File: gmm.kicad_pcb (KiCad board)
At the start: 6 copper layers, 70 x 50 mm, 213 parts, among them P1 10144518-061802LF, P2 10144518-061802LF, P3 10144518-061802LF, P4 10144518-061802LF, P5 10144518-061802LF, U1 CCGM1A1, U10 PCA9539AHF, U11 TPS3840DL28DBV, U2 5P49V6965, U3 LM26480SQ, U4 STG3692, U5 STG3692, U6 74LVC1G08, U7 74LVC1G07, U8 STG3692, U9 IS25LQ032B-JNLE, Y1 NX3225SA

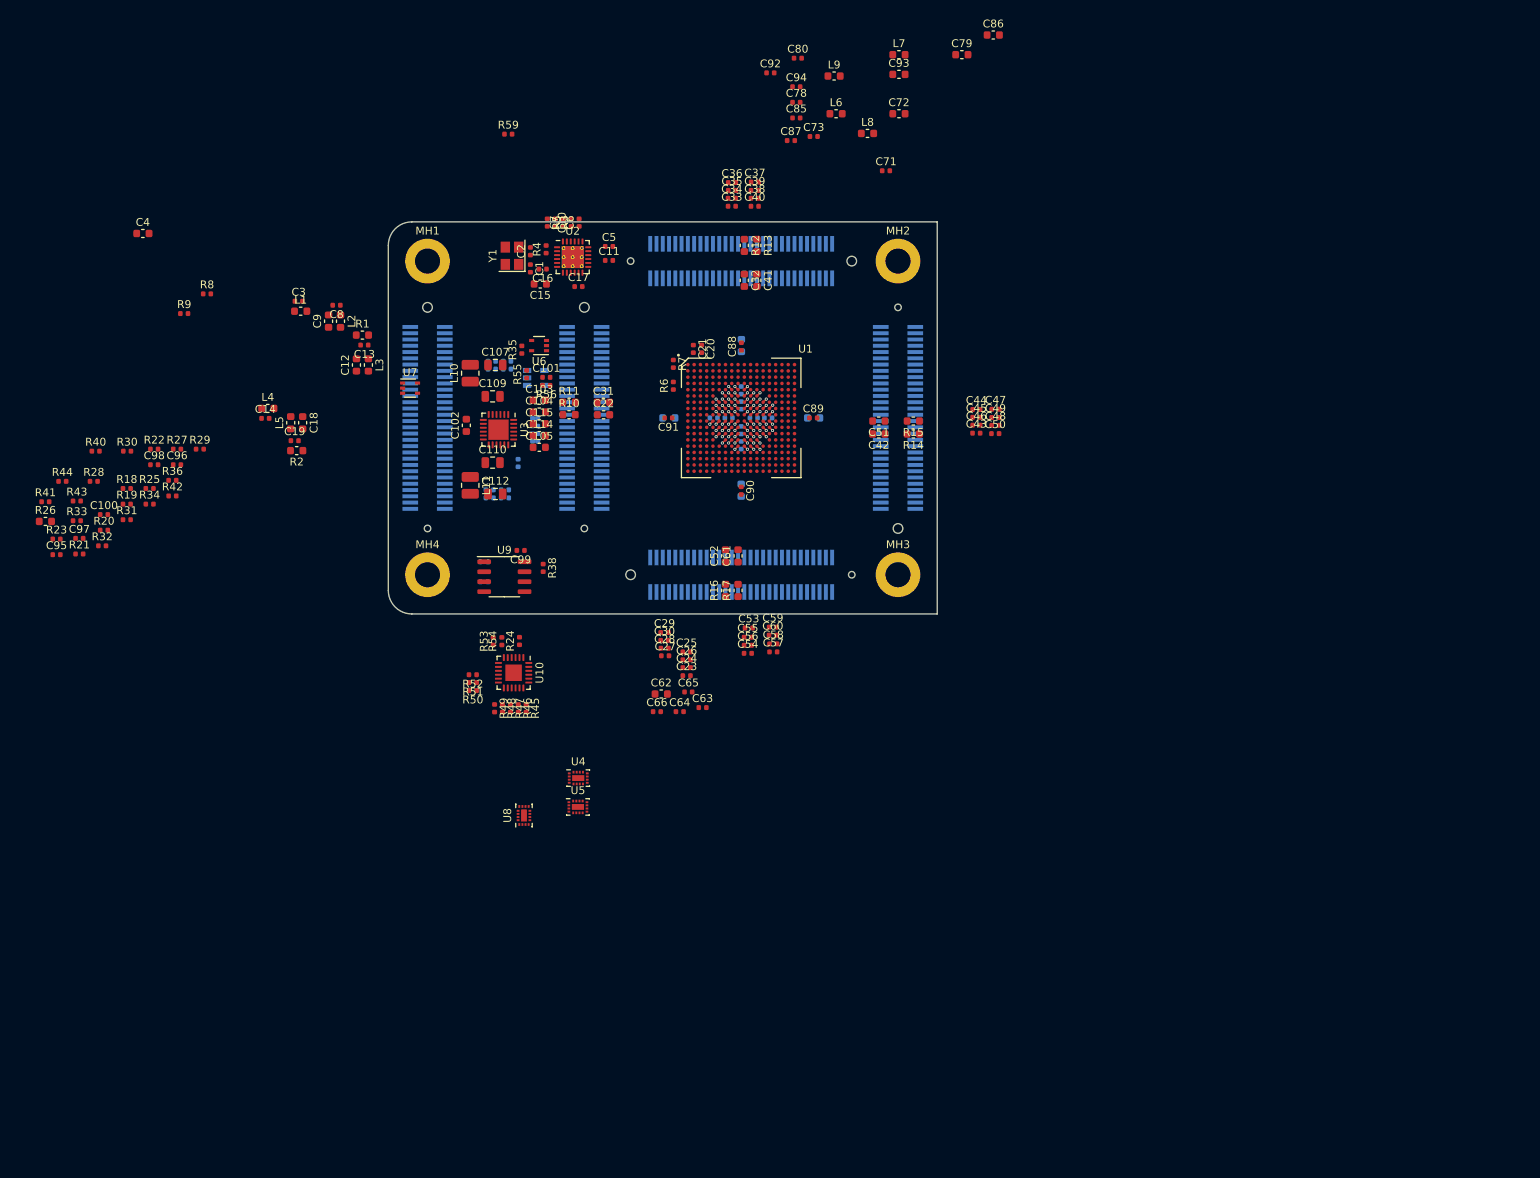
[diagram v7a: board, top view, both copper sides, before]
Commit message: Add footprints for solder jumpers and L10 inductor
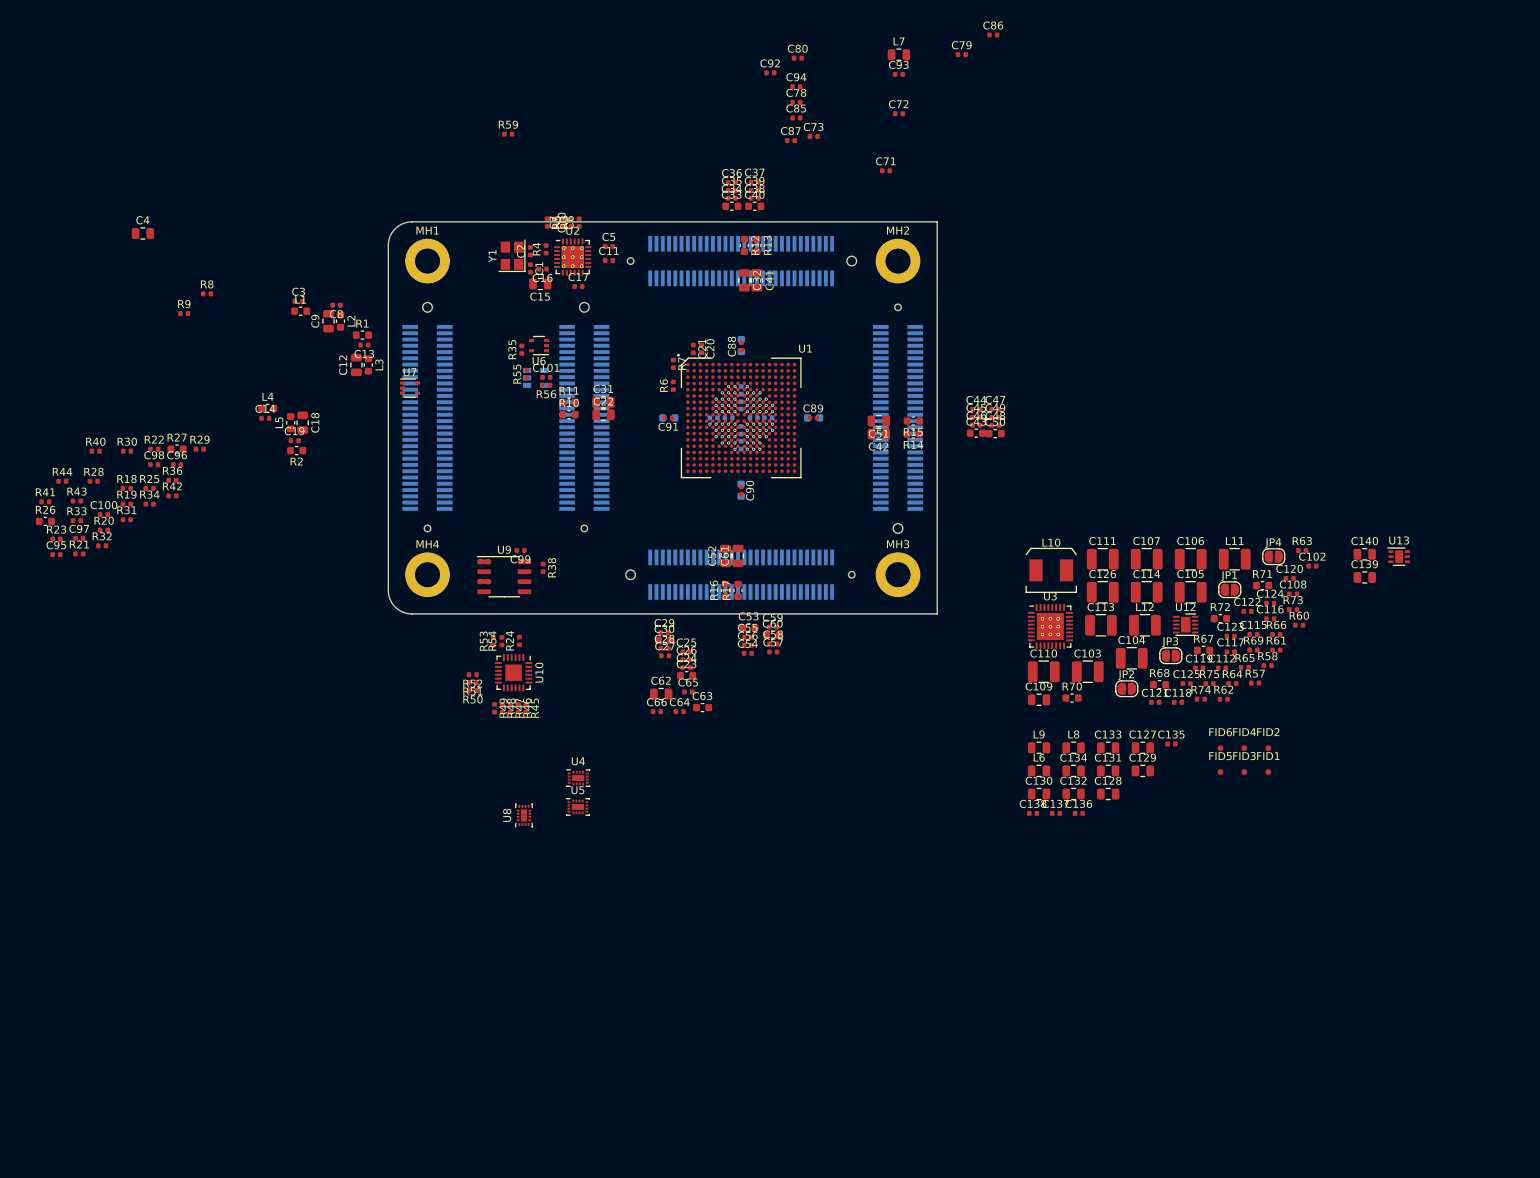
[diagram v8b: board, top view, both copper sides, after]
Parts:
- added C116: 0.01uF, Capacitor_SMD:C_0402_1005Metric, F.Cu at (202.5, 130.6)
- added C117: 0.01uF, Capacitor_SMD:C_0402_1005Metric, F.Cu at (197.4, 134.8)
- added C118: DNI, Capacitor_SMD:C_0402_1005Metric, F.Cu at (190.7, 141.3)
- added C119: 1000pF, Capacitor_SMD:C_0402_1005Metric, F.Cu at (193.4, 136.9)
- added C120: DNI, Capacitor_SMD:C_0402_1005Metric, F.Cu at (204.9, 125.5)
- added C121: 1000pF, Capacitor_SMD:C_0402_1005Metric, F.Cu at (187.8, 141.3)
- added C122: 0.01uF, Capacitor_SMD:C_0402_1005Metric, F.Cu at (199.6, 129.7)
- added C123: DNI, Capacitor_SMD:C_0402_1005Metric, F.Cu at (197.4, 132.8)
- added C124: 1000pF, Capacitor_SMD:C_0402_1005Metric, F.Cu at (202.5, 128.6)
- added C125: 0.1uF, Capacitor_SMD:C_0402_1005Metric, F.Cu at (191.8, 138.9)
- added C126: 22uF, Capacitor_SMD:C_1210_3225Metric, F.Cu at (181.1, 127.2)
- added C127: 2.2uF, Capacitor_SMD:C_0805_2012Metric, F.Cu at (186.2, 147.1)
- added C128: 2.2uF, Capacitor_SMD:C_0805_2012Metric, F.Cu at (181.8, 153.0)
- added C129: 2.2uF, Capacitor_SMD:C_0805_2012Metric, F.Cu at (186.2, 150.0)
- added C130: 2.2uF, Capacitor_SMD:C_0805_2012Metric, F.Cu at (173.0, 153.0)
- added C131: 2.2uF, Capacitor_SMD:C_0805_2012Metric, F.Cu at (181.8, 150.0)
- added C132: 2.2uF, Capacitor_SMD:C_0805_2012Metric, F.Cu at (177.4, 153.0)
- added C133: 2.2uF, Capacitor_SMD:C_0805_2012Metric, F.Cu at (181.8, 147.1)
- added C134: 2.2uF, Capacitor_SMD:C_0805_2012Metric, F.Cu at (177.4, 150.0)
- added C135: 0.1uF, Capacitor_SMD:C_0402_1005Metric, F.Cu at (189.9, 146.6)
- added C136: 0.1uF, Capacitor_SMD:C_0402_1005Metric, F.Cu at (178.1, 155.4)
- added C137: 0.01uF, Capacitor_SMD:C_0402_1005Metric, F.Cu at (175.1, 155.4)
- added C138: 0.01uF, Capacitor_SMD:C_0402_1005Metric, F.Cu at (172.2, 155.4)
- added C139: 2.2uF, Capacitor_SMD:C_0805_2012Metric, F.Cu at (214.5, 125.3)
- added C140: 2.2uF, Capacitor_SMD:C_0805_2012Metric, F.Cu at (214.5, 122.4)
- added FID1: Fiducial, Fiducial:Fiducial_0.75mm_Mask1.5mm, F.Cu at (202.2, 150.2)
- added FID2: Fiducial, Fiducial:Fiducial_0.75mm_Mask1.5mm, F.Cu at (202.2, 147.1)
- added FID3: Fiducial, Fiducial:Fiducial_0.75mm_Mask1.5mm, F.Cu at (199.2, 150.2)
- added FID4: Fiducial, Fiducial:Fiducial_0.75mm_Mask1.5mm, F.Cu at (199.2, 147.1)
- added FID5: Fiducial, Fiducial:Fiducial_0.75mm_Mask1.5mm, F.Cu at (196.1, 150.2)
- added FID6: Fiducial, Fiducial:Fiducial_0.75mm_Mask1.5mm, F.Cu at (196.1, 147.1)
- added JP1: SolderJumper_2_Open_Small, Jumper:SolderJumper-2_P1.3mm_Open_RoundedPad1.0x1.5mm, F.Cu at (197.3, 126.9)
- added JP2: SolderJumper_2_Open_Small, Jumper:SolderJumper-2_P1.3mm_Open_RoundedPad1.0x1.5mm, F.Cu at (184.2, 139.5)
- added JP3: SolderJumper_2_Open_Small, Jumper:SolderJumper-2_P1.3mm_Open_RoundedPad1.0x1.5mm, F.Cu at (189.8, 135.3)
- added JP4: SolderJumper_2_Open_Small, Jumper:SolderJumper-2_P1.3mm_Open_RoundedPad1.0x1.5mm, F.Cu at (202.9, 122.7)
- added L12: 2.2uH, Inductor_SMD:L_1210_3225Metric, F.Cu at (186.5, 131.4)
- added R67: 10k, Resistor_SMD:R_0603_1608Metric, F.Cu at (194.0, 134.6)
- added R68: 20k, Resistor_SMD:R_0603_1608Metric, F.Cu at (188.4, 139.0)
- added R69: 2k, Resistor_SMD:R_0402_1005Metric, F.Cu at (200.3, 134.6)
- added R70: 0, Resistor_SMD:R_0603_1608Metric, F.Cu at (177.2, 140.7)
- added R71: DNI, Resistor_SMD:R_0603_1608Metric, F.Cu at (201.5, 126.4)
- added R72: 20k, Resistor_SMD:R_0603_1608Metric, F.Cu at (196.1, 130.6)
- added R73: 2k, Resistor_SMD:R_0402_1005Metric, F.Cu at (205.4, 129.4)
- added R74: 2k, Resistor_SMD:R_0402_1005Metric, F.Cu at (193.6, 140.9)
- added R75: 16k, Resistor_SMD:R_0402_1005Metric, F.Cu at (194.7, 138.9)
- added U12: TPS7A91, Package_DFN_QFN:Texas_S-PDSO-N10_EP1.2x2mm, F.Cu at (191.7, 131.4)
- added U13: ADP151ACP, Package_DFN_QFN:DFN-6-1EP_2x2mm_P0.65mm_EP1x1.6mm, F.Cu at (218.9, 122.7)
- C10, C11, C16, C17, C24, C25, C26, C27, C28, C29, C34, C35, C36, C37, C38, C39, C44, C45, C46, C47, C48, C49, C5, C54, C55, C56, C57, C58, C59, C6, C64, C65, C66, C7, C74, C75, C81, C82, C88, C89: value 0.01uF -> 0.1uF
- C102: value 1.0uF -> 0.047uF; footprint Capacitor_SMD:C_0603_1608Metric -> Capacitor_SMD:C_0402_1005Metric
- C103, C104, C105, C114: value 1.0uF -> 22uF; footprint Capacitor_SMD:C_0603_1608Metric -> Capacitor_SMD:C_1210_3225Metric
- C106: value 15pF -> 22uF; footprint Capacitor_SMD:C_0402_1005Metric -> Capacitor_SMD:C_1210_3225Metric; moved to F.Cu
- C107, C110: value 10uF -> 22uF; footprint Capacitor_SMD:C_0805_2012Metric -> Capacitor_SMD:C_1210_3225Metric
- C108: value DNI -> 0.047uF; moved to F.Cu
- C109: value 10uF -> 2.2uF
- C111: value 8.2pF -> 22uF; footprint Capacitor_SMD:C_0402_1005Metric -> Capacitor_SMD:C_1210_3225Metric; moved to F.Cu
- C112: value 10uF -> 0.047uF; footprint Capacitor_SMD:C_0805_2012Metric -> Capacitor_SMD:C_0402_1005Metric
- C113: value DNI -> 22uF; footprint Capacitor_SMD:C_0402_1005Metric -> Capacitor_SMD:C_1210_3225Metric; moved to F.Cu
- C115: value 1.0uF -> 0.01uF; footprint Capacitor_SMD:C_0603_1608Metric -> Capacitor_SMD:C_0402_1005Metric
- C12, C15, C18, C22, C31, C32, C4, C41, C42, C51, C52, C61, C62, C9: value 1.0uF -> 2.2uF; footprint Capacitor_SMD:C_0603_1608Metric -> Capacitor_SMD:C_0805_2012Metric
- C23, C30, C33, C40, C43, C50, C53, C60, C63: value 0.01uF -> 0.47uF; footprint Capacitor_SMD:C_0402_1005Metric -> Capacitor_SMD:C_0603_1608Metric
- C67, C68, C69, C70: value 1.0uF -> 0.47uF
- C72, C79, C86, C93: value 1.0uF -> 0.1uF; footprint Capacitor_SMD:C_0603_1608Metric -> Capacitor_SMD:C_0402_1005Metric
- L10: footprint Inductor_SMD:L_1008_2520Metric -> gmm:L_Murata_FDSD0518_5.2x4.9mm
- L11: footprint Inductor_SMD:L_1008_2520Metric -> Inductor_SMD:L_1210_3225Metric
- L6, L7, L8, L9: value 4.7uH -> 600 Ohm @100MHz, 1.5A; footprint Inductor_SMD:L_0603_1608Metric -> Inductor_SMD:L_0805_2012Metric
- R27: footprint Resistor_SMD:R_0402_1005Metric -> Resistor_SMD:R_0603_1608Metric
- R37, R38, R39: value 4.7k -> 10k
- R57, R58: value 100k -> 2.49k; moved to F.Cu
- R60: value 402k -> 23.7k; moved to F.Cu
- R61: value 100k -> 7.5k; moved to F.Cu
- R62: value 10k -> 7.5k; moved to F.Cu
- R63, R64: value 100k -> 15k; moved to F.Cu
- R65, R66: value 100k -> 10k; moved to F.Cu
- U3: value LM26480SQ -> TPS65266; footprint Package_DFN_QFN:WQFN-24-1EP_4x4mm_P0.5mm_EP2.6x2.6mm -> Package_DFN_QFN:Texas_S-PVQFN-N32_EP3.45x3.45mm_ThermalVias
- moved C102 109.4 mm to (207.9, 123.9), turned to 0 degrees
- moved R57 105.6 mm to (200.5, 138.8)
- moved R60 104.5 mm to (206.2, 131.4)
- moved R58 104.5 mm to (202.1, 136.6)
- moved C108 104.3 mm to (205.4, 127.5)
- moved R61 100.3 mm to (203.2, 134.6)
- moved R63 99.2 mm to (206.5, 121.9), turned to 0 degrees
- moved R66 98.0 mm to (203.2, 132.6), turned to 0 degrees
- moved L11 97.9 mm to (197.9, 123.0), turned to 0 degrees
- moved R65 96.1 mm to (199.2, 136.8), turned to 0 degrees
- moved C112 95.3 mm to (196.3, 136.9)
- moved C115 95.0 mm to (200.3, 132.6)
- moved R62 94.9 mm to (196.5, 140.9), turned to 0 degrees
- moved R64 94.0 mm to (197.6, 138.9), turned to 0 degrees
- moved C106 92.4 mm to (192.3, 123.0)
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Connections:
- C102 pad 1: V_IN -> Net-(C102-Pad1)
- C102 pad 2: GND -> Net-(C102-Pad2)
- C104 pad 1: +2V5 -> V_IN
- C105 pad 1: +2V5 -> V_IN
- C106 pad 2: Net-(C106-Pad2) -> GND
- C108 pad 1: Net-(C106-Pad2) -> Net-(C108-Pad1)
- C108 pad 2: GND -> Net-(C108-Pad2)
- C110 pad 1: V_IN -> +2V5
- C111 pad 2: Net-(C111-Pad2) -> GND
- C112 pad 1: +2V5 -> Net-(C112-Pad1)
- C112 pad 2: GND -> Net-(C112-Pad2)
- C113 pad 1: Net-(C111-Pad2) -> /Power Converter/V_1P5
- C114 pad 1: V_1P0_A1 -> /Power Converter/V_1P5
- C115 pad 1: V_1P0_A2 -> Net-(C115-Pad1)
- C14 pad 1: +2V5 -> /Clock and SERDES/VDD_PLL
- C71 pad 1: V_1P0_A1 -> V_1P0_A
- C78 pad 1: V_1P0_A1 -> V_1P0_A
- C8 pad 1: +2V5 -> /Clock and SERDES/VDD_PLL
- C85 pad 1: V_1P0_A2 -> V_1P0_A
- C93 pad 1: Net-(C93-Pad1) -> VDD_CLK
- C94 pad 1: Net-(C93-Pad1) -> VDD_CLK
- L10 pad 1: Net-(L10-Pad1) -> Net-(C102-Pad1)
- L11 pad 1: Net-(L11-Pad1) -> Net-(C108-Pad1)
- L2 pad 1: +2V5 -> /Clock and SERDES/VDD_PLL
- L4 pad 1: +2V5 -> /Clock and SERDES/VDD_PLL
- L6 pad 1: V_1P0_A1 -> V_1P0_A
- L7 pad 1: V_1P0_A1 -> V_1P0_A
- L8 pad 1: V_1P0_A2 -> V_1P0_A
- L9 pad 1: +2V5 -> VDD_CLK
- L9 pad 2: Net-(C93-Pad1) -> +2V5
- R26 pad 2: +2V5 -> VDD_CLK
- R57 pad 2: Net-(C106-Pad2) -> Net-(JP1-Pad2)
- R58 pad 1: Net-(C106-Pad2) -> Net-(JP1-Pad2)
- R58 pad 2: GND -> Net-(JP2-Pad2)
- R60 pad 2: Net-(C111-Pad2) -> Net-(R60-Pad2)
- R61 pad 1: Net-(C111-Pad2) -> Net-(JP2-Pad2)
- R61 pad 2: GND -> Net-(R61-Pad2)
- R62 pad 1: +2V5 -> Net-(R60-Pad2)
- R62 pad 2: Net-(R62-Pad2) -> GND
- R63 pad 1: V_1P0_A1 -> Net-(R61-Pad2)
- R63 pad 2: Net-(R63-Pad2) -> GND
- R64 pad 1: Net-(R63-Pad2) -> /Power Converter/V_1P5
- R64 pad 2: GND -> Net-(R64-Pad2)
- R65 pad 1: V_1P0_A2 -> Net-(R65-Pad1)
- R65 pad 2: Net-(R65-Pad2) -> GND
- R66 pad 1: Net-(R65-Pad2) -> Net-(R64-Pad2)
- U1 pad E4: Net-(C93-Pad1) -> VDD_CLK
- U3 pad 1: V_IN -> GND
- U3 pad 10: V_IN -> Net-(C108-Pad1)
- U3 pad 11: Net-(C111-Pad2) -> GND
- U3 pad 12: OFF_N -> V_IN
- U3 pad 14: Net-(L11-Pad1) -> GND
- U3 pad 15: GND -> Net-(C112-Pad1)
- U3 pad 16: Net-(R62-Pad2) -> Net-(C112-Pad2)
- U3 pad 17: Net-(R62-Pad2) -> Net-(C117-Pad1)
- U3 pad 18: GND -> /Power Converter/COMP3
- U3 pad 19: +2V5 -> Net-(R64-Pad2)
- U3 pad 20: V_1P0_A1 -> Net-(R65-Pad1)
- U3 pad 21: Net-(R63-Pad2) -> GND
- U3 pad 22: Net-(R65-Pad2) -> Net-(R61-Pad2)
- U3 pad 23: V_1P0_A2 -> /Power Converter/COMP1
- U3 pad 24: +2V5 -> Net-(C115-Pad1)
- U3 pad 25: GND -> Net-(C102-Pad2)
- U3 pad 3: POR_N -> GND
- U3 pad 4: GND -> POR_N
- U3 pad 5: Net-(L10-Pad1) -> V_IN
- U3 pad 6: V_IN -> Net-(R60-Pad2)
- U3 pad 7: OFF_N -> /Power Converter/COMP2
- U3 pad 8: Net-(C106-Pad2) -> Net-(C116-Pad1)
- U3 pad 9: GND -> Net-(C108-Pad2)
